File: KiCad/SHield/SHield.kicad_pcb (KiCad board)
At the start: 2 copper layers, 68.6 x 53.3 mm, 18 parts, among them J1 Conn_01x08_Female, J2 Conn_01x04_Female, J3 Conn_01x04_Female, P1 Power, P2 Analog, P3 Digital, P4 Digital, P5 CONN_01X01, P6 CONN_01X01, P7 CONN_01X01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

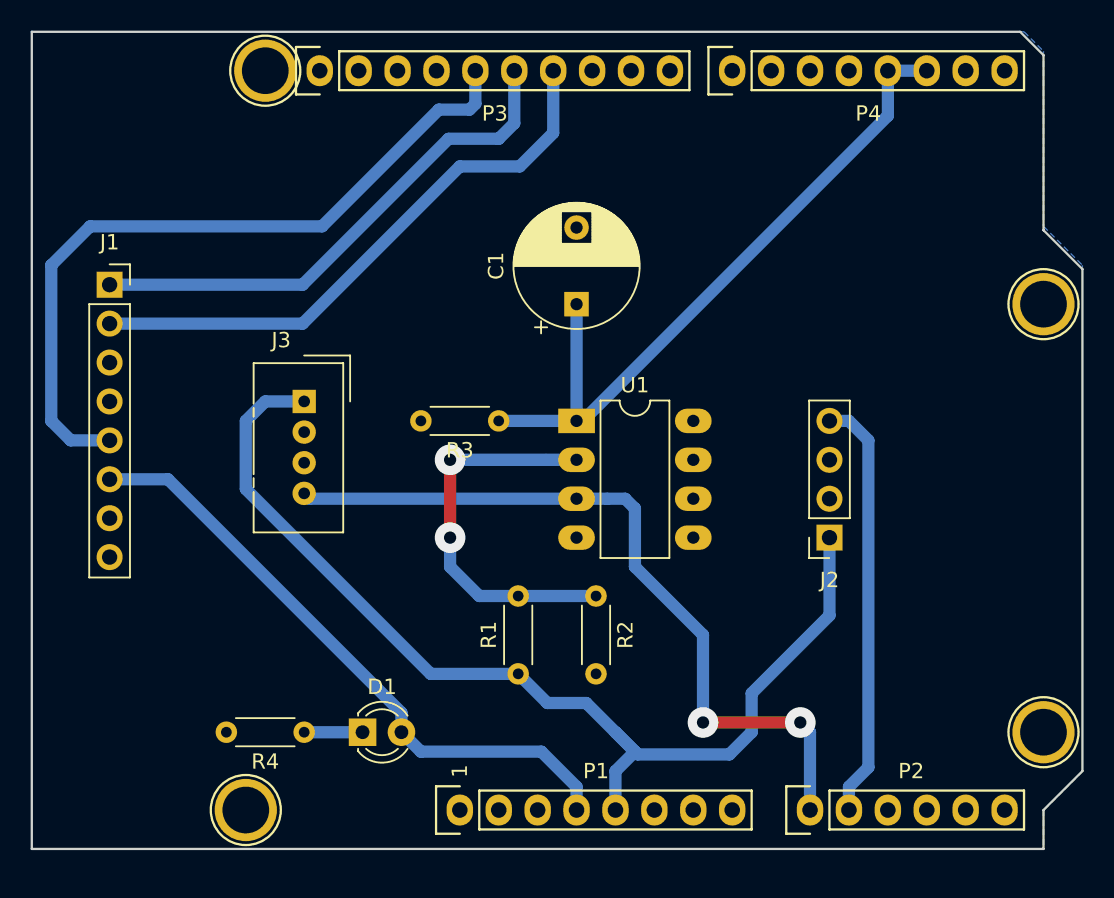
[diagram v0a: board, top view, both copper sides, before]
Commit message: ajout shield capteur gaz SB
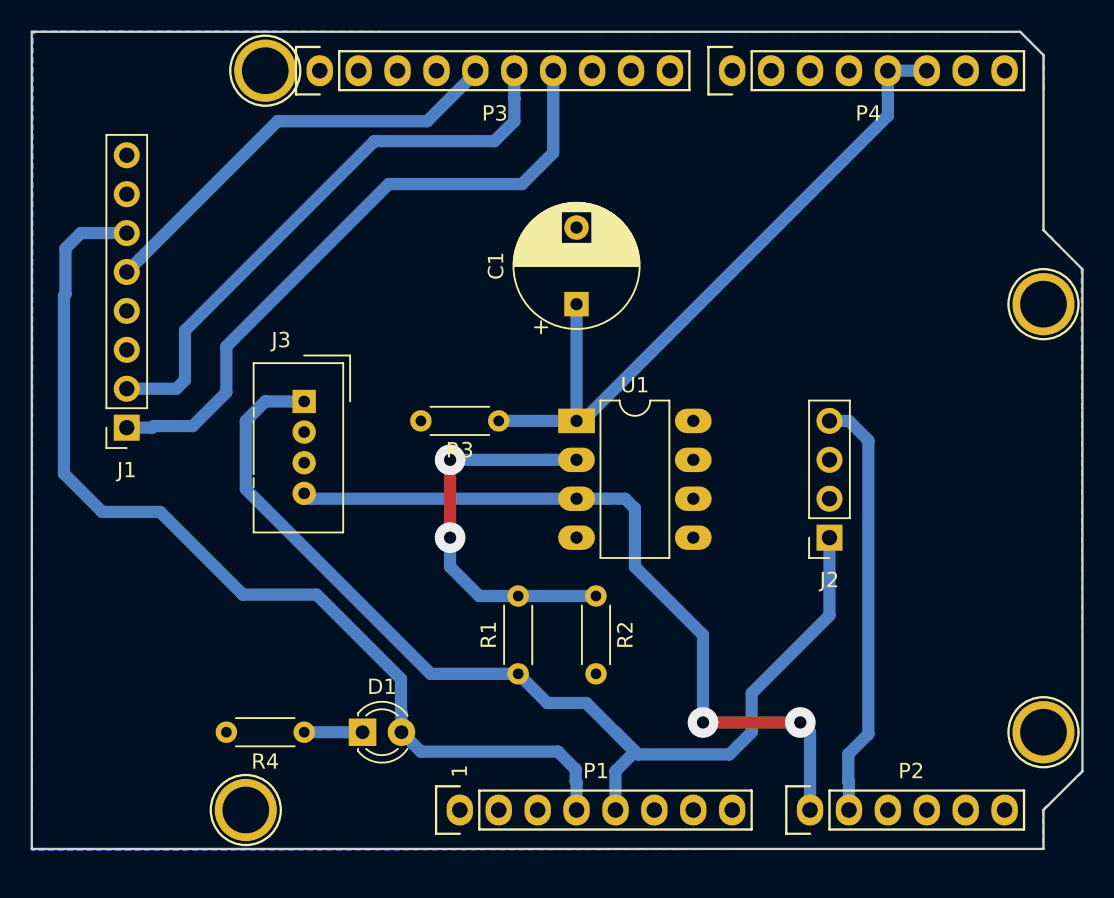
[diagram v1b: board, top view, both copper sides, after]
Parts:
- moved J1 9.40 mm to (117.2, 98.9), turned to 180 degrees
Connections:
- J1 pad 1: /12(MISO) -> /11(**/MOSI)
- J1 pad 2: /11(**/MOSI) -> /12(MISO)
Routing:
- net +3V3: track 41.2 -> 65.4 mm
- net /13(SCK): track 48.7 -> 28.3 mm
- net /11(**/MOSI): track 38.2 -> 42.4 mm
- net /12(MISO): track 34.2 -> 37.7 mm

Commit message: modification et ajout carte pour capteur en salle blanche
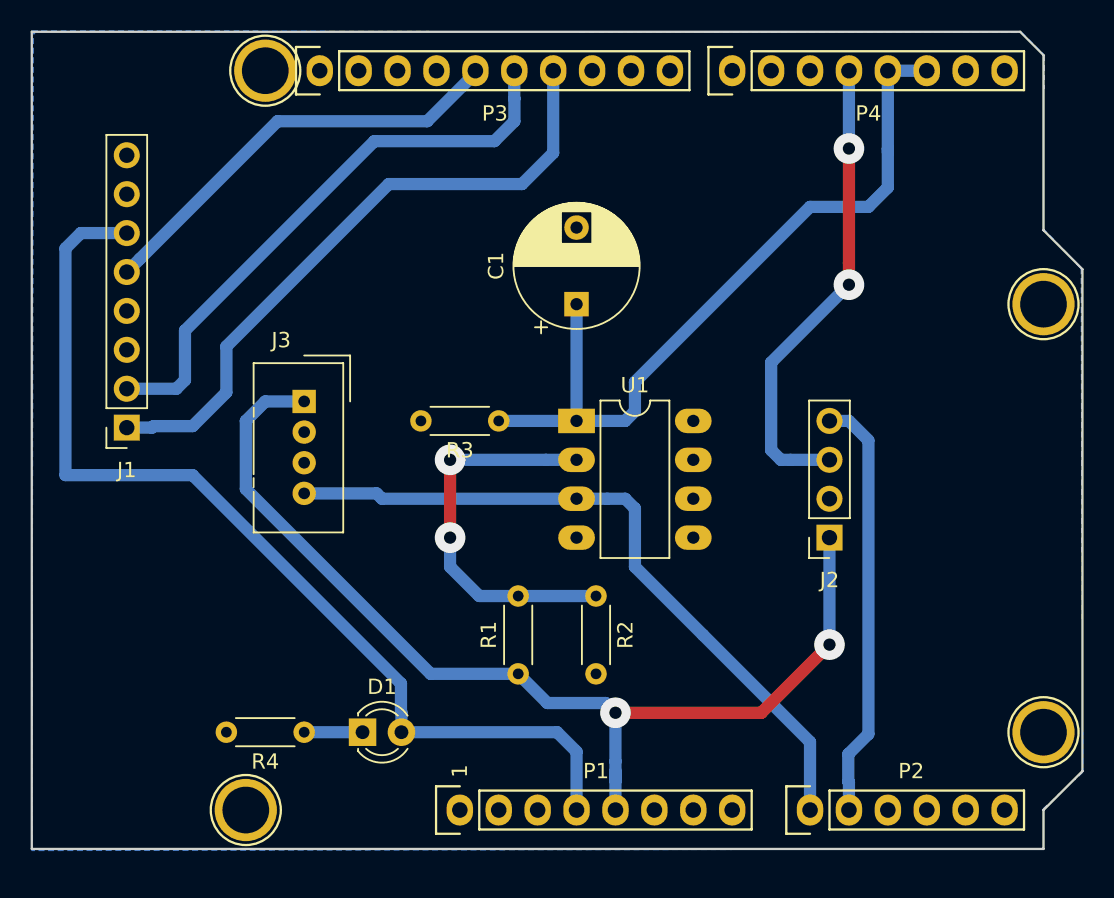
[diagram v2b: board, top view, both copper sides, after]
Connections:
- J2 pad 3: Net-(J2-Pad3) -> /4
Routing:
- net /4: track 0.00 -> 30.9 mm, vias 0 -> 2
- net /2: track 46.8 -> 51.3 mm
- net /A0: track 50.1 -> 46.4 mm, vias 2 -> 0
- net +5V: track 70.5 -> 68.7 mm, vias 0 -> 2

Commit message: Modifications deu shield, ajout de deux LED
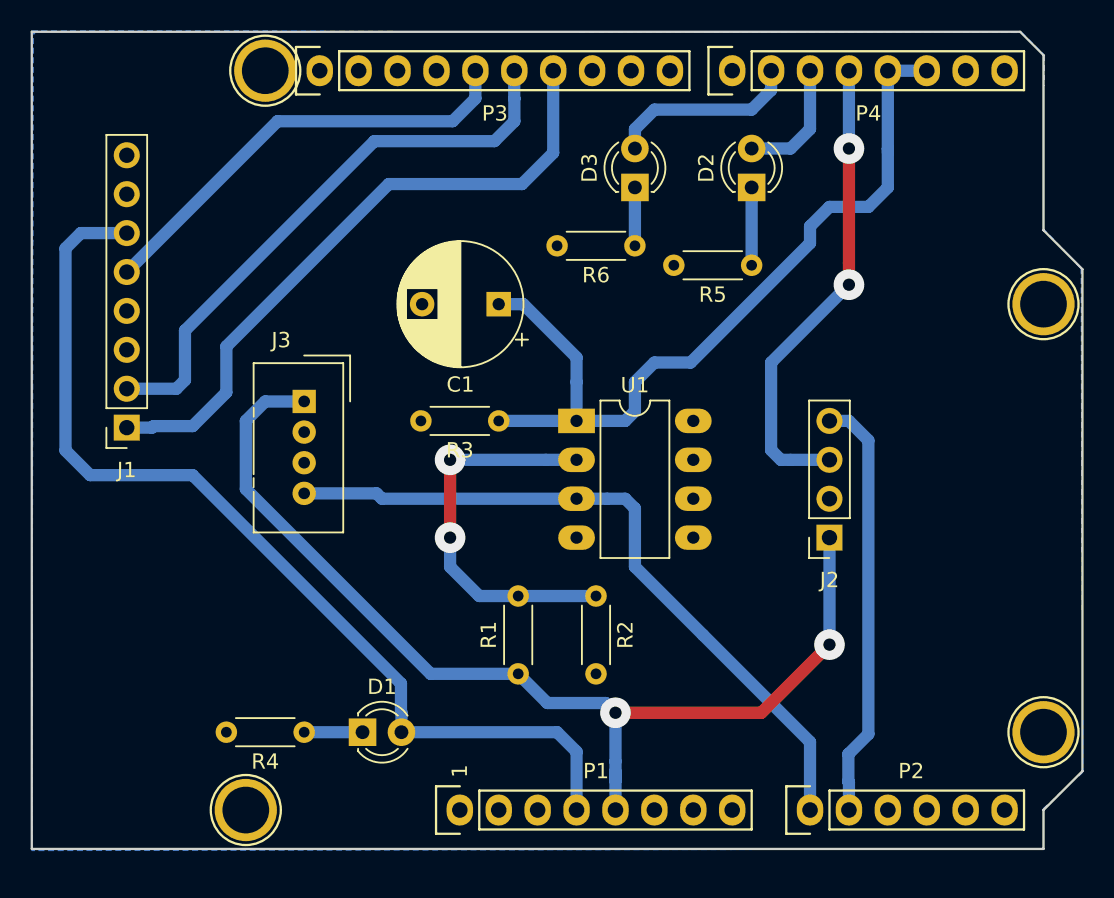
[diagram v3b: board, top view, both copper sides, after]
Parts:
- added D2: LED, LED_THT:LED_D3.0mm_FlatTop, F.Cu at (158.0, 83.2)
- added D3: LED, LED_THT:LED_D3.0mm_FlatTop, F.Cu at (150.4, 83.2)
- added R5: R, Resistor_THT:R_Axial_DIN0204_L3.6mm_D1.6mm_P5.08mm_Horizontal, F.Cu at (158.0, 88.3)
- added R6: R, Resistor_THT:R_Axial_DIN0204_L3.6mm_D1.6mm_P5.08mm_Horizontal, F.Cu at (150.4, 87.0)
- moved C1 5.08 mm to (141.5, 90.8), turned to 180 degrees
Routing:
- net /6(**): track 0.00 -> 12.5 mm
- net /5(**): track 0.00 -> 8.15 mm
- net Net-(D2-Pad1): track 0.00 -> 5.08 mm
- net Net-(D3-Pad1): track 0.00 -> 3.81 mm
- net /2: track 51.3 -> 55.0 mm
- net /13(SCK): track 28.3 -> 29.3 mm
- net +3V3: track 65.9 -> 64.9 mm

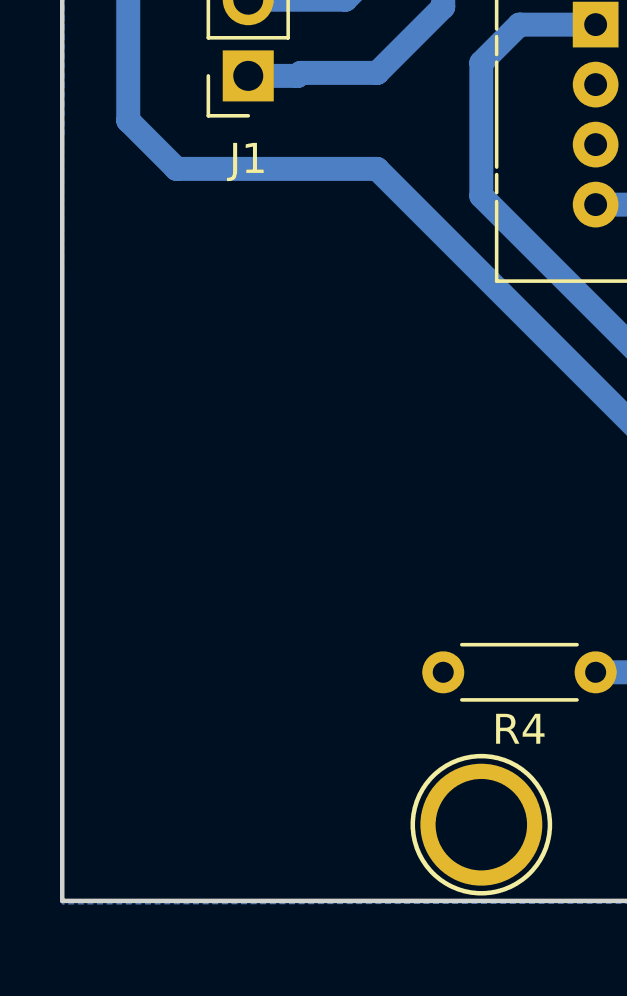
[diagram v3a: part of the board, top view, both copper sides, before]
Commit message: Ajout du text sur les pcbs
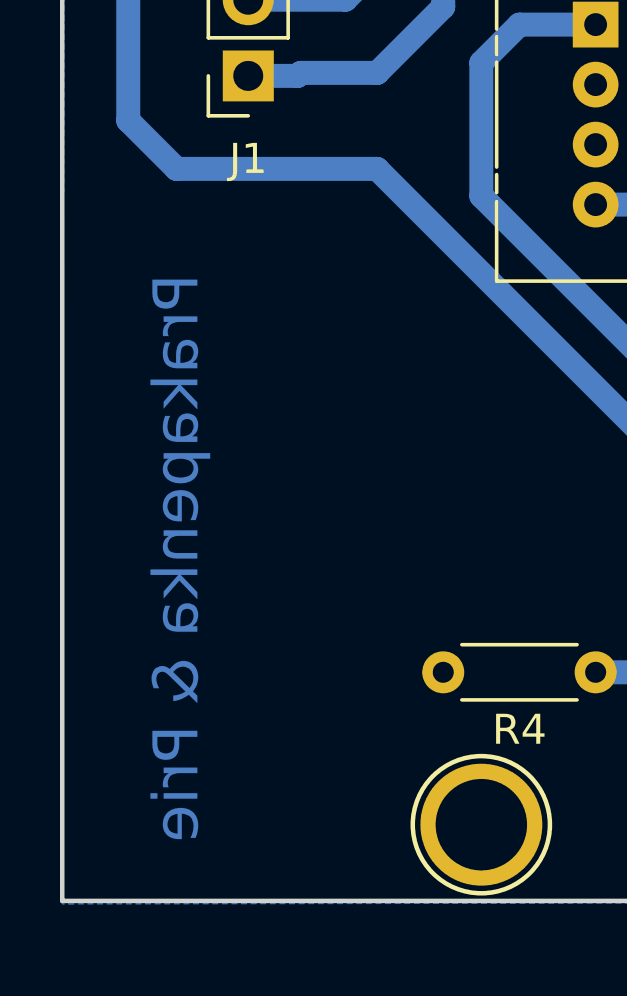
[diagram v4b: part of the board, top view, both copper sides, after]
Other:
- board text added: "Prakapenka & Prie"
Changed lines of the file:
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@@
   (general
     (thickness 1.6)
-    (drawings 27)
+    (drawings 28)
     (tracks 120)
     (zones 0)
@@
     )
   )
+  (gr_text "Prakapenka & Prie" (at 114.808 114.935 90) (layer B.Cu)
+    (effects (font (size 1.5 1.5) (thickness 0.3)) (justify mirror))
+  )
   (gr_text 1 (at 138.938 121.285 90) (layer F.SilkS)
